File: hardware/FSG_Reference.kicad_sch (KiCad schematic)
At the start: 49 parts, among them J3 Screw_Terminal_01x02, K1 SANYOU_SRD_Form_C, Q1 BSS138, Q2 Si2319CDS, Q3 BSS138, U1 LM393, U2 LM393, U3 LM393, U5 LM393, U6 74AHC1G02

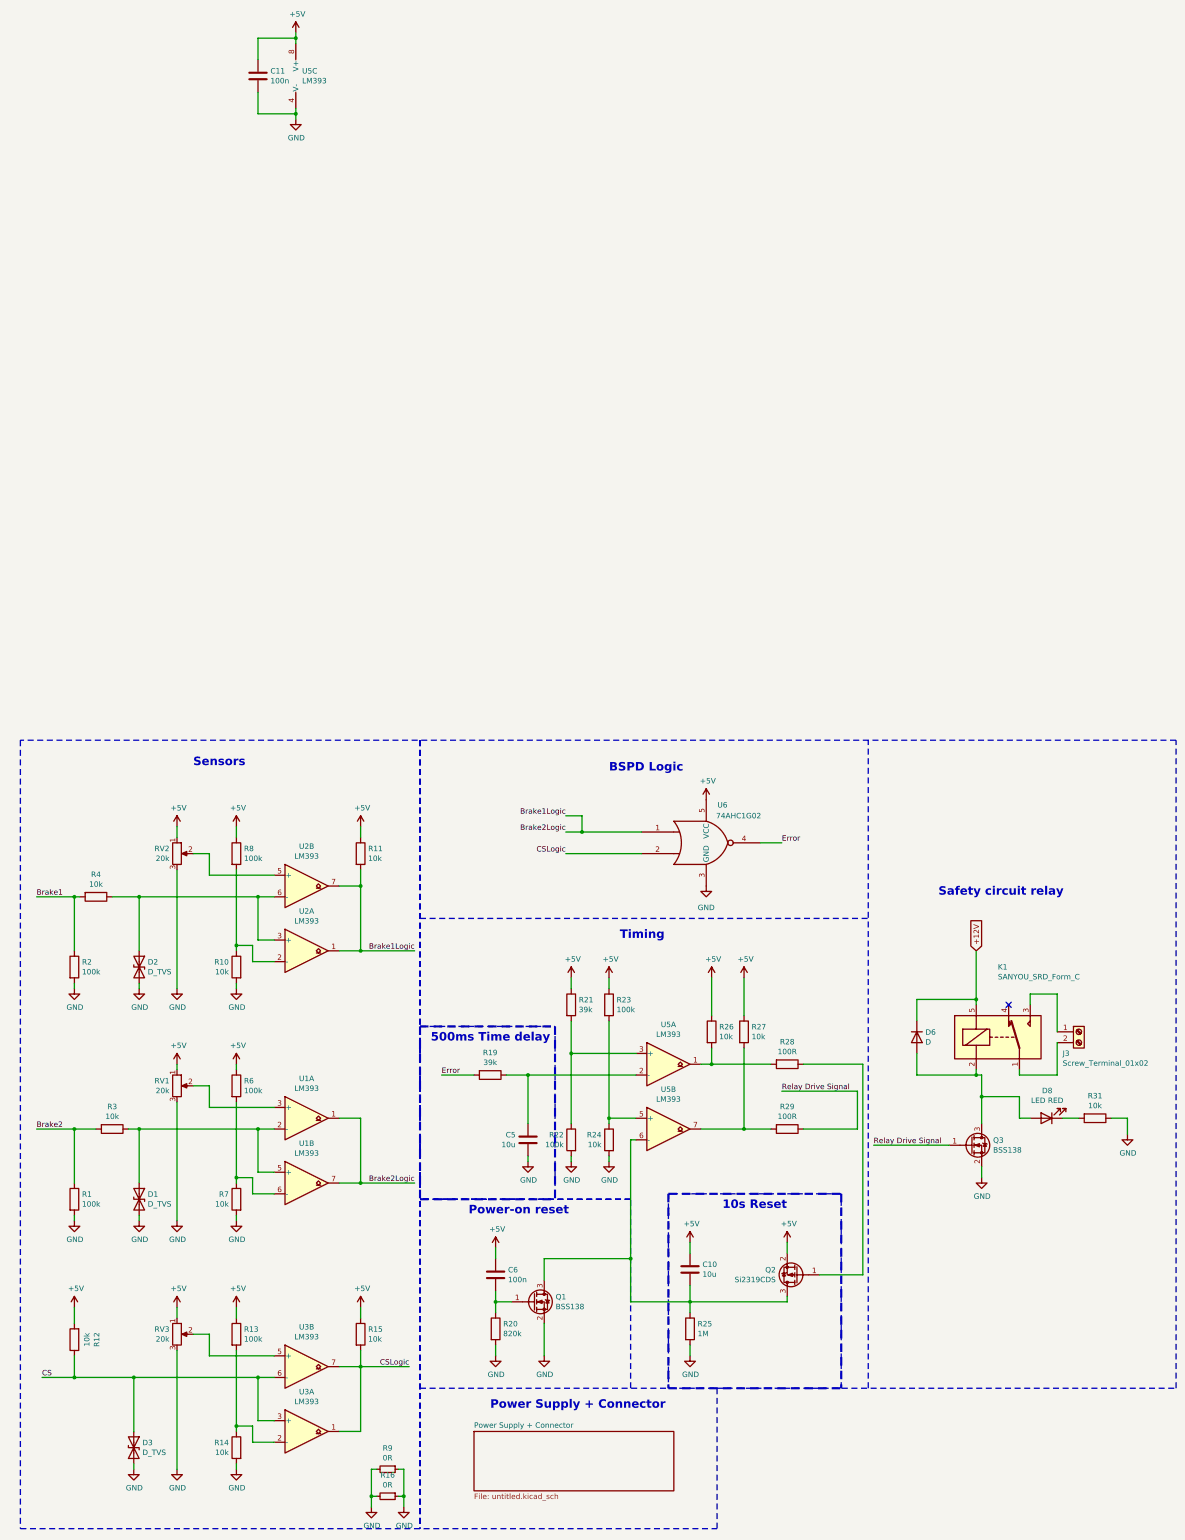
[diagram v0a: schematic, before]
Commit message: Changed the connector
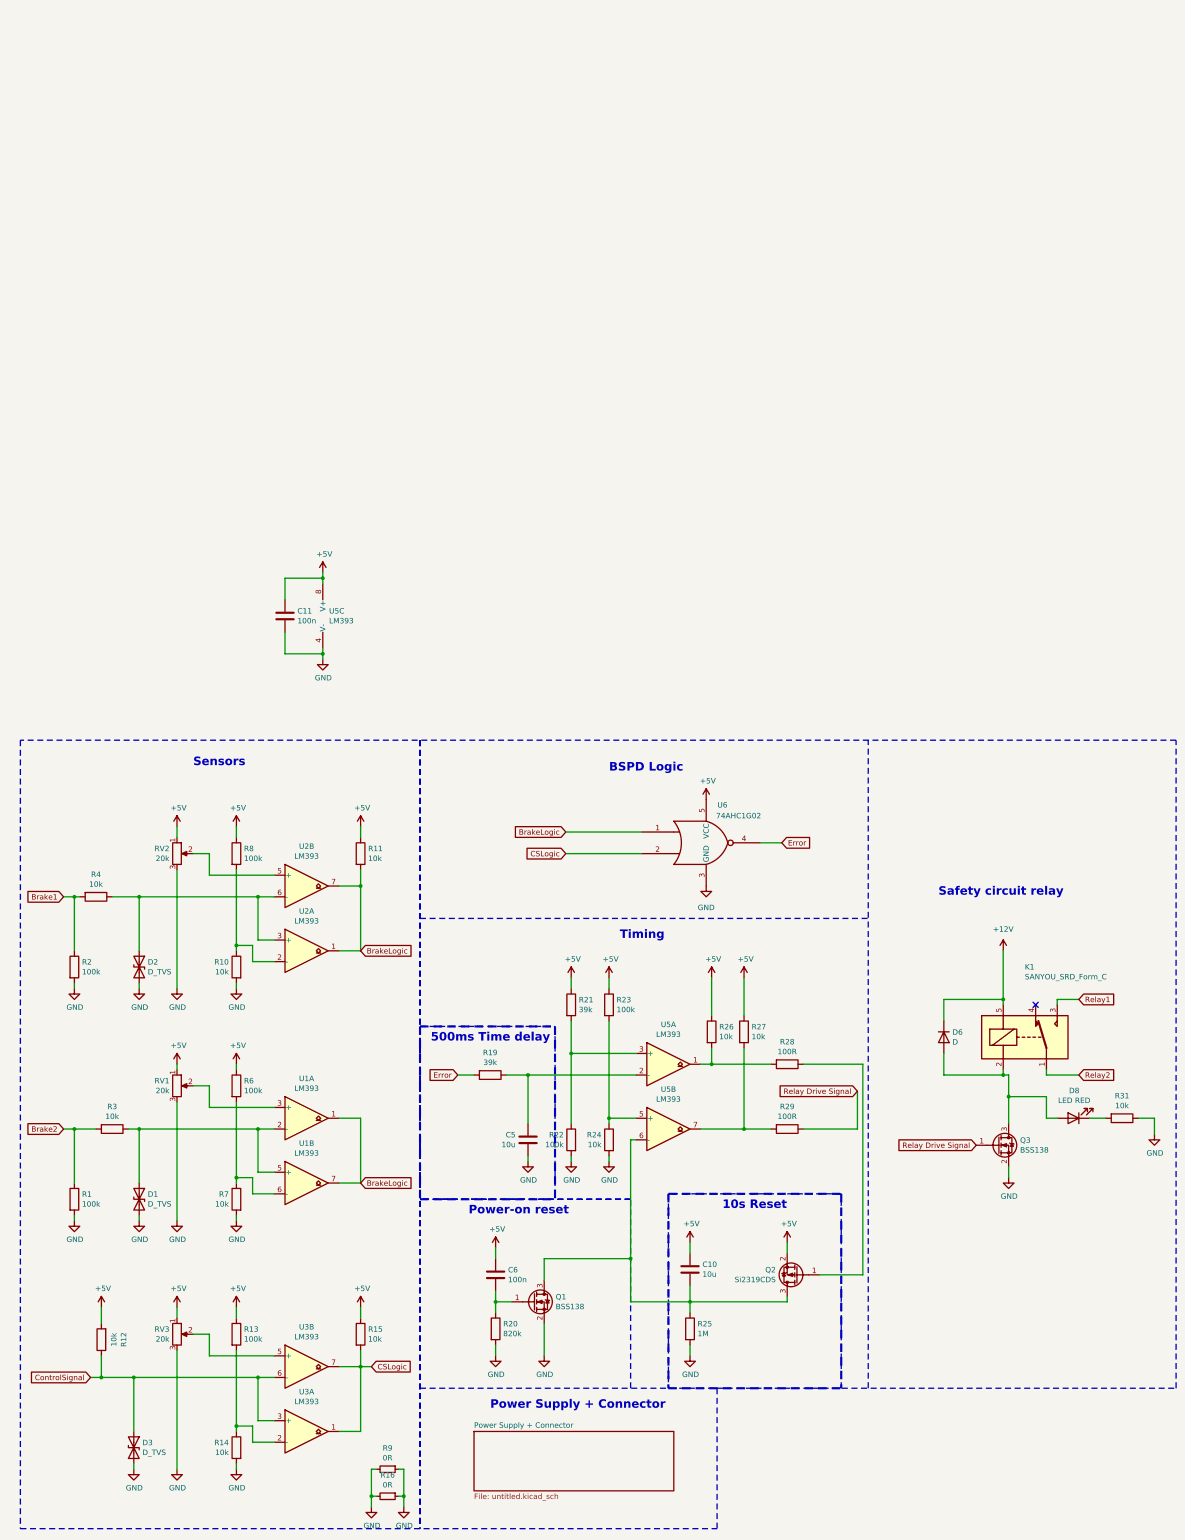
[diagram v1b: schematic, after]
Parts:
- removed J3: Screw_Terminal_01x02, Connector_Molex:Molex_Micro-Fit_3.0_43650-0200_1x02_P3.00mm_Horizontal, symbol Connector:Screw_Terminal_01x02
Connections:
- net Relay1: now reaches K1.3
- net Relay2: now reaches K1.1
- net Brake1Logic renamed BrakeLogic
- net CS renamed ControlSignal
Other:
- moved on the sheet: C11, D6, D8, K1, Q3, R12, R31, U5C

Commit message: New BSPD Layout based on BSPD by Jakub Drankiewicz in 2021
-Schematic needs to be adjusted for better understanding
-Comparator of Current Sensor removed, the one on Current Sensor Board is sufficient
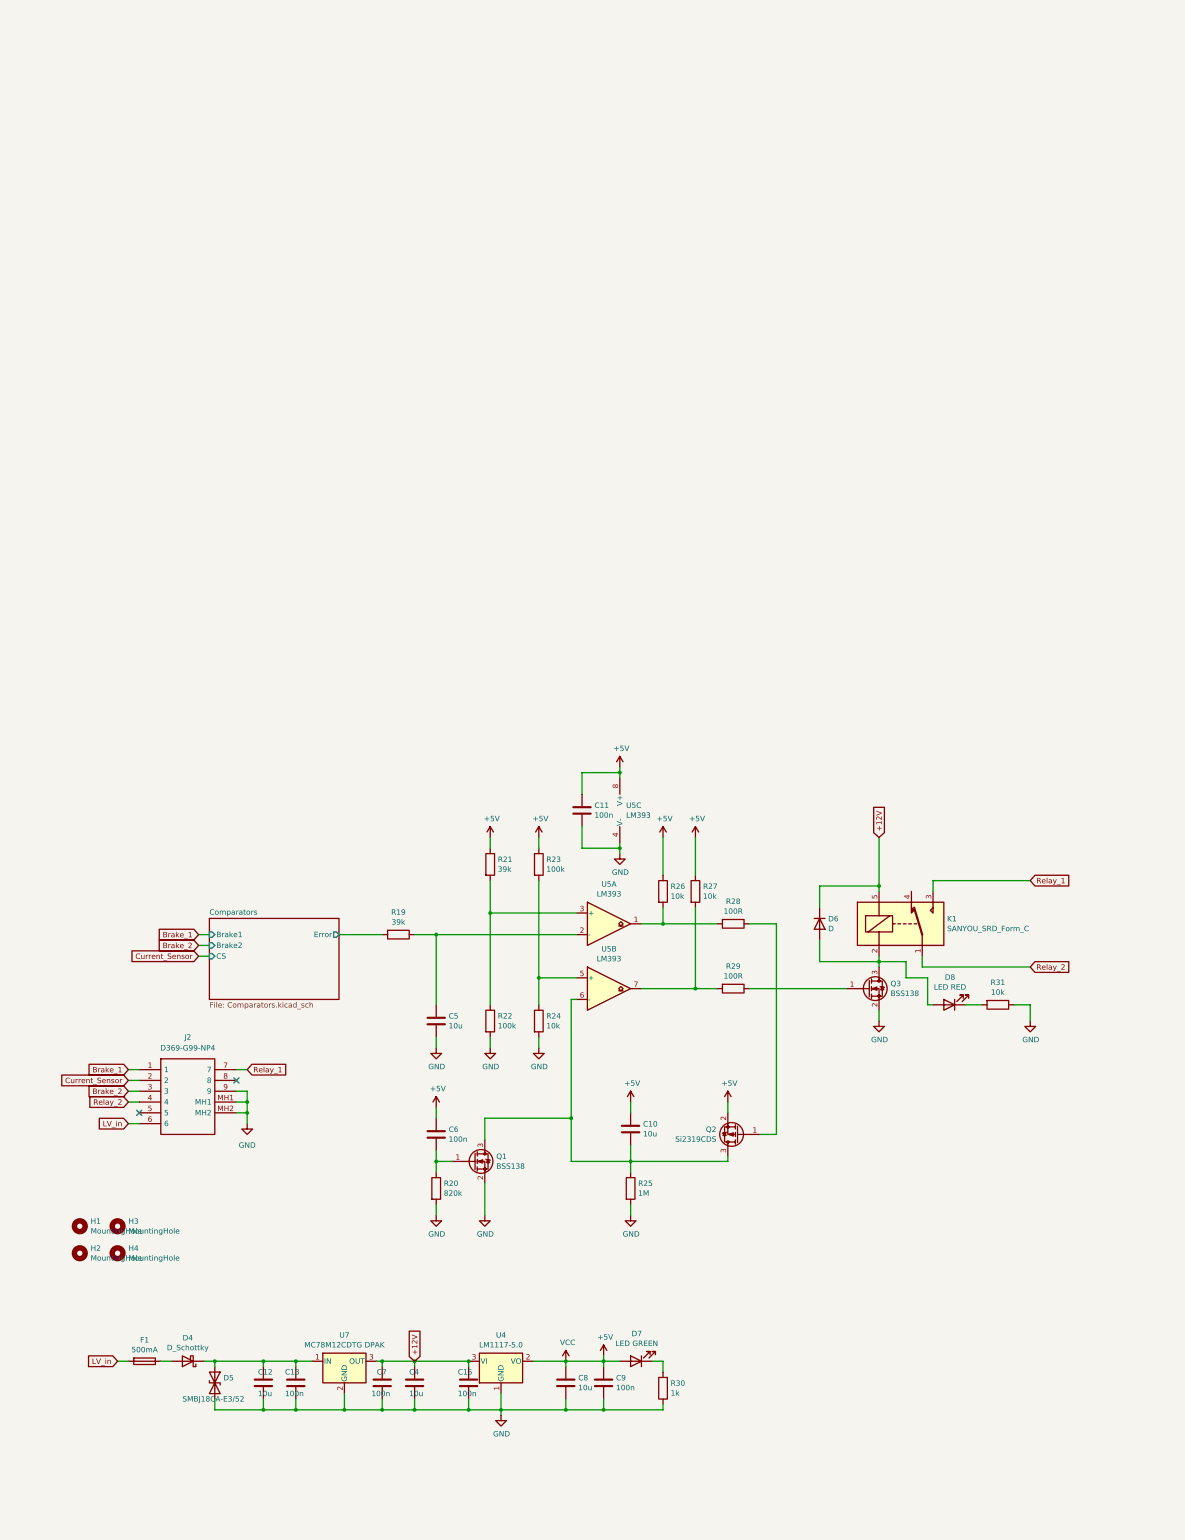
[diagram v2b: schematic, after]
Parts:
- removed D1, D2, D3: D_TVS, Diode_SMD:D_SMB, symbol Device:D_TVS
- removed R1, R13, R2, R6, R8: 100k, Resistor_SMD:R_1206_3216Metric, symbol Device:R
- removed R10, R11, R12, R14, R15, R3, R4, R7: 10k, Resistor_SMD:R_1206_3216Metric, symbol Device:R
- removed R16, R9: 0R, Resistor_SMD:R_1206_3216Metric, symbol Device:R_Small
- removed RV1, RV2, RV3: 20k, Potentiometer_THT:Potentiometer_ACP_CA9-H2,5_Horizontal, symbol Device:R_POT
- removed U1, U2, U3: LM393, Package_SO:SOIC-8_3.9x4.9mm_P1.27mm, symbol Comparator:LM393
- removed U6: 74AHC1G02, Package_TO_SOT_SMD:SOT-353_SC-70-5, symbol 74xGxx:74AHC1G02
- added C12, C4, C8: 10u, Capacitor_SMD:C_1206_3216Metric, symbol Device:C
- added C13, C15, C7, C9: 100n, Capacitor_SMD:C_1206_3216Metric, symbol Device:C
- added D4: D_Schottky, Diode_SMD:D_SMB, symbol Device:D_Schottky
- added D5: SMBJ18CA-E3/52, Diode_SMD:D_SMB, symbol Device:D_TVS
- added D7: LED GREEN, Capacitor_SMD:C_1206_3216Metric, symbol Device:LED
- added F1: 500mA, Fuse:Fuse_1206_3216Metric, symbol Device:Fuse
- added H1, H2, H3, H4: MountingHole, MountingHole:MountingHole_3.2mm_M3_ISO7380, symbol Mechanical:MountingHole
- added J2: D369-G99-NP4, Connector_9pin:D369G99NP4, symbol D369-G99-NP4:D369-G99-NP4
- added R30: 1k, Resistor_SMD:R_1206_3216Metric, symbol Device:R
- added U4: LM1117-5.0, Package_TO_SOT_SMD:SOT-223, symbol Regulator_Linear:LM1117-5.0
- added U7: MC78M12CDTG DPAK, Package_TO_SOT_SMD:TO-252-3_TabPin2, symbol Regulator_Linear:L7812
- D8: footprint LED_SMD:LED_PLCC-2 -> Capacitor_SMD:C_1206_3216Metric
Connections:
- net +12V: now also C15.1, C4.1, C7.1, U4.3 (VI), U7.3 (OUT)
- net +5V: now also C8.1, C9.1, D7.2 (A), U4.2 (VO)
- net GND: now also C12.2, C13.2, C15.2, C4.2, C7.2, C8.2, C9.2, D5.2 (A2), J2.9, J2.MH1, J2.MH2, R30.1, U4.1 (GND), U7.2 (GND)
- net Error renamed Comparators/Error
- net Relay Drive Signal: no longer names the net of Q3.1 (G), R29.1
- net Relay1 renamed Relay_1
- net Relay_1: now also J2.7
- net Relay2 renamed Relay_2
- net Relay_2: now also J2.4
- new net: D7.1 (K), R30.2
- new net: D4.2 (A), F1.1
- new net: C12.1, C13.1, D4.1 (K), D5.1 (A1), U7.1 (IN)
- new net Brake_1: J2.1
- new net Brake_2: J2.3
- new net Current_Sensor: J2.2
- new net LV_in: F1.2, J2.6
- no-connect marks 1 -> 2
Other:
- removed sheet Power Supply + Connector
- added sheet Comparators (Comparators.kicad_sch)
- note removed: "10s Reset"
- note removed: "500ms Time delay"
- note removed: "BSPD Logic"
- note removed: "Power Supply + Connector"
- note removed: "Power-on reset"
- note removed: "Safety circuit relay"
- note removed: "Sensors"
- note removed: "Timing"
- moved on the sheet: C10, C11, C5, C6, D6, D8, K1, Q1, Q2, Q3, R19, R20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
